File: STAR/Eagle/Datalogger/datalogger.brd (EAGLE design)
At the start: 26.4 x 55.9 mm, 9 parts, among them U1 MT25QL01GBBB8ESF-0AAT

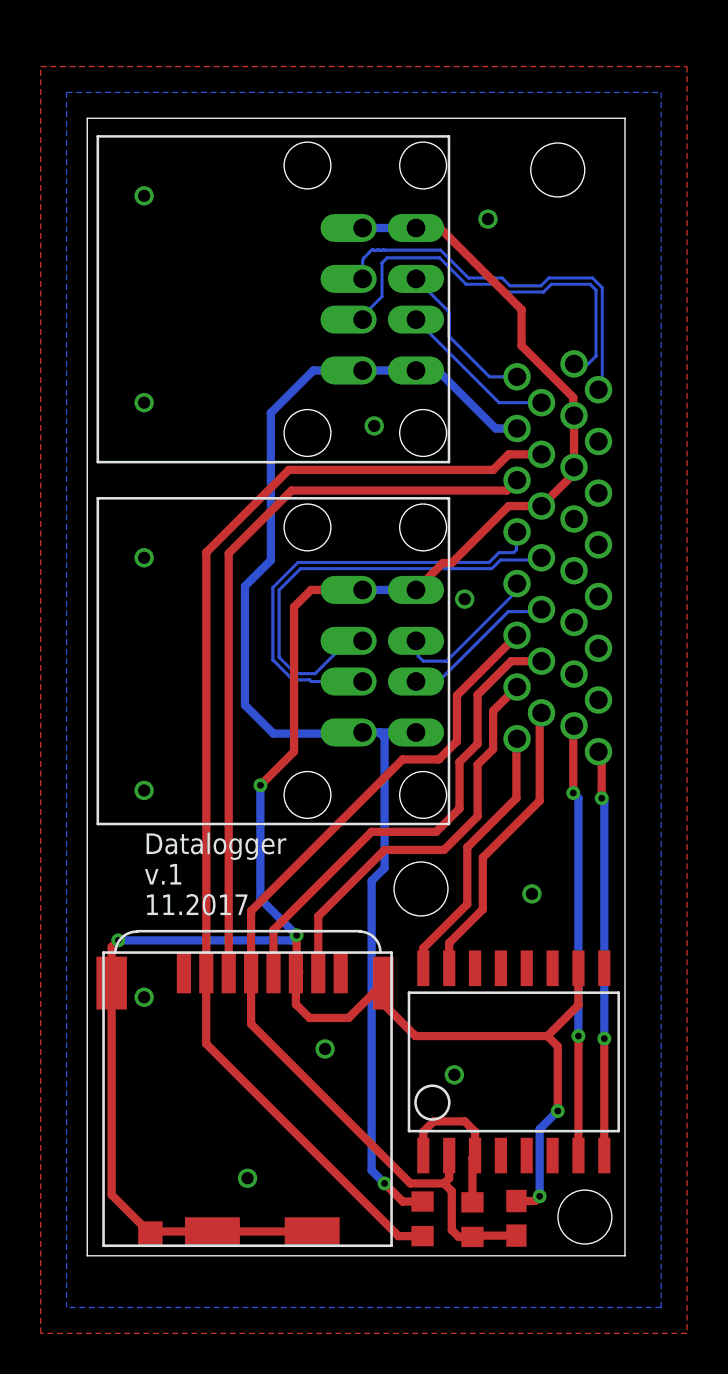
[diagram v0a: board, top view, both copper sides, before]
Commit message: fixed routing shit on datalogger:
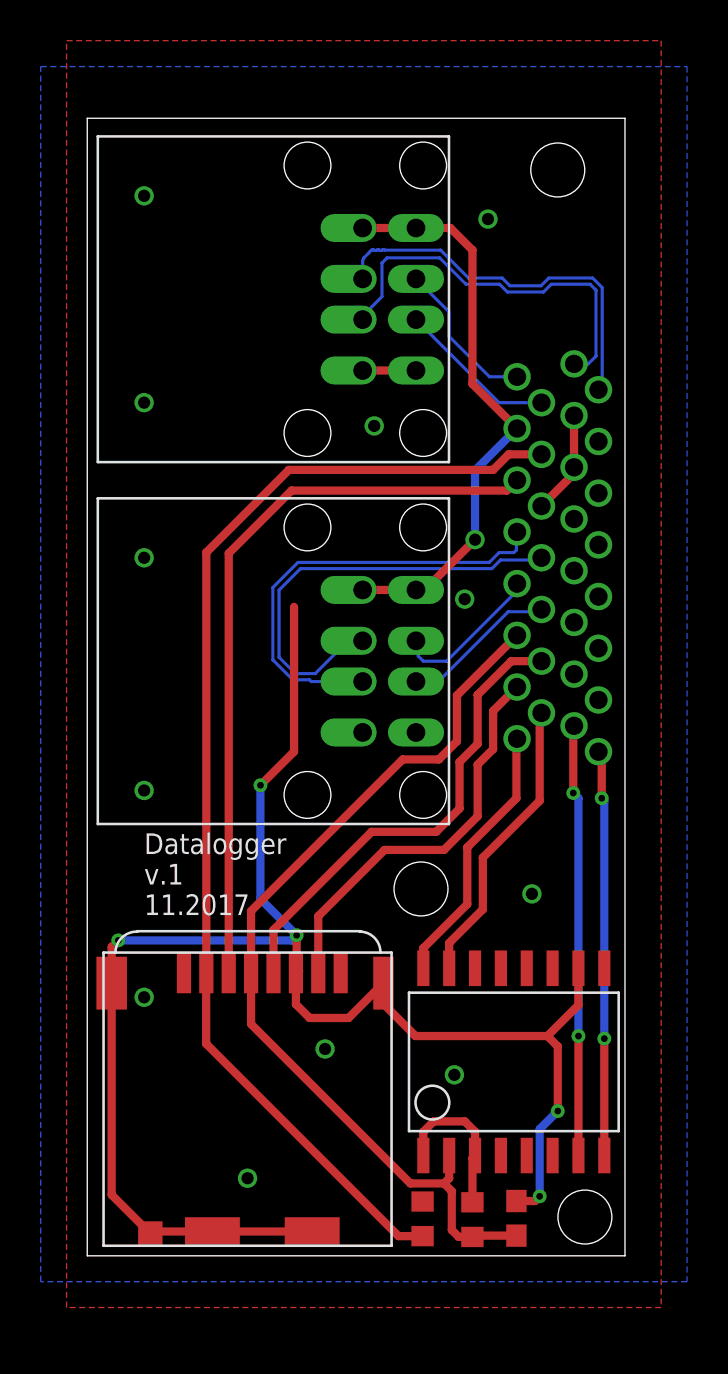
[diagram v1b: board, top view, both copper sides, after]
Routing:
- net +5V: track 63.0 -> 28.4 mm
- net GND: track 117.4 -> 90.1 mm
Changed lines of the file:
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@@
 </class>
 </classes>
-<designrules name="OshPark *">
+<designrules name="OshPark">
 <description language="de">&lt;b&gt;EAGLE Design Rules&lt;/b&gt;
 &lt;p&gt;
@@
 <param name="mlMinCreamFrame" value="0mil"/>
 <param name="mlMaxCreamFrame" value="0mil"/>
-<param name="mlViaStopLimit" value="25mil"/>
+<param name="mlViaStopLimit" value="0mil"/>
 <param name="srRoundness" value="0"/>
 <param name="srMinRoundness" value="0mil"/>
@@
 <contactref element="U$2" pad="GND1"/>
 <contactref element="CONNECTOR" pad="14"/>
-<wire x1="0.575" y1="35.25" x2="3.195" y2="35.25" width="0.4064" layer="16"/>
-<wire x1="0.575" y1="17.47" x2="3.195" y2="17.47" width="0.4064" layer="16"/>
 <wire x1="-2.7042" y1="-1.3447" x2="-2.7042" y2="-2.8838" width="0.4064" layer="1"/>
 <wire x1="-2.7042" y1="-2.8838" x2="-2.032" y2="-3.556" width="0.4064" layer="1"/>
@@
 <wire x1="-11.7542" y1="-1.8447" x2="-11.7542" y2="-12.2447" width="0.4064" layer="1"/>
 <wire x1="-11.7542" y1="-12.2447" x2="-9.8542" y2="-14.1447" width="0.4064" layer="1"/>
-<wire x1="3.195" y1="35.25" x2="4.374" y2="35.25" width="0.4064" layer="1"/>
-<wire x1="4.374" y1="35.25" x2="8.382" y2="31.242" width="0.4064" layer="1"/>
-<wire x1="8.382" y1="31.242" x2="8.382" y2="29.464" width="0.4064" layer="1"/>
-<wire x1="8.382" y1="29.464" x2="10.922" y2="26.924" width="0.4064" layer="1"/>
-<wire x1="10.922" y1="26.924" x2="10.922" y2="26.073" width="0.4064" layer="1"/>
 <wire x1="10.922" y1="26.073" x2="10.96" y2="26.035" width="0.4064" layer="1"/>
-<wire x1="9.36" y1="21.59" x2="7.747" y2="21.59" width="0.4064" layer="1"/>
-<wire x1="7.747" y1="21.59" x2="4.953" y2="18.796" width="0.4064" layer="1"/>
-<wire x1="4.953" y1="18.796" x2="4.521" y2="18.796" width="0.4064" layer="1"/>
-<wire x1="4.521" y1="18.796" x2="3.195" y2="17.47" width="0.4064" layer="1"/>
-<wire x1="0.575" y1="17.47" x2="-1.961" y2="17.47" width="0.4064" layer="1"/>
-<wire x1="-1.961" y1="17.47" x2="-2.794" y2="16.637" width="0.4064" layer="1"/>
 <wire x1="-2.794" y1="16.637" x2="-2.794" y2="9.525" width="0.4064" layer="1"/>
 <wire x1="-2.794" y1="9.525" x2="-4.445" y2="7.874" width="0.4064" layer="1"/>
@@
 <wire x1="9.271" y1="-12.319" x2="9.271" y2="-9.017" width="0.4064" layer="16"/>
 <wire x1="9.271" y1="-9.017" x2="10.16" y2="-8.128" width="0.4064" layer="16"/>
-<polygon width="0.4064" layer="1">
-<vertex x="-15.24" y="43.18"/>
-<vertex x="16.51" y="43.18"/>
-<vertex x="16.51" y="-19.05"/>
-<vertex x="-15.24" y="-19.05"/>
-</polygon>
-<polygon width="0.4064" layer="16">
-<vertex x="-13.97" y="41.91"/>
-<vertex x="15.24" y="41.91"/>
-<vertex x="15.24" y="-17.78"/>
-<vertex x="-13.97" y="-17.78"/>
-</polygon>
 <via x="-10.16" y="36.83" extent="1-16" drill="0.6"/>
 <via x="-10.16" y="26.67" extent="1-16" drill="0.6"/>
@@
 <via x="-5.08" y="-11.43" extent="1-16" drill="0.6"/>
 <via x="5.08" y="-6.35" extent="1-16" drill="0.6"/>
+<wire x1="0.575" y1="28.25" x2="3.195" y2="28.25" width="0.4064" layer="1"/>
+<polygon width="0.4064" layer="16">
+<vertex x="-15.24" y="43.18"/>
+<vertex x="16.51" y="43.18"/>
+<vertex x="16.51" y="-16.51"/>
+<vertex x="-15.24" y="-16.51"/>
+</polygon>
+<polygon width="0.4064" layer="1">
+<vertex x="-13.97" y="44.45"/>
+<vertex x="15.24" y="44.45"/>
+<vertex x="15.24" y="-17.78"/>
+<vertex x="-13.97" y="-17.78"/>
+</polygon>
 </signal>
 <signal name="+3V3">
@@
 <contactref element="R2" pad="2"/>
 <contactref element="CONNECTOR" pad="29"/>
-<wire x1="0.575" y1="28.25" x2="3.195" y2="28.25" width="0.4064" layer="16"/>
-<wire x1="3.195" y1="28.25" x2="4.262" y2="28.25" width="0.4064" layer="16"/>
-<wire x1="4.262" y1="28.25" x2="7.112" y2="25.4" width="0.4064" layer="16"/>
-<wire x1="7.112" y1="25.4" x2="8.16" y2="25.4" width="0.4064" layer="16"/>
-<wire x1="3.195" y1="10.47" x2="1.397" y2="10.47" width="0.4064" layer="16"/>
-<wire x1="1.397" y1="10.47" x2="0.575" y2="10.47" width="0.4064" layer="16"/>
-<wire x1="0.575" y1="28.25" x2="-1.849" y2="28.25" width="0.4064" layer="16"/>
-<wire x1="-1.849" y1="28.25" x2="-3.937" y2="26.162" width="0.4064" layer="16"/>
-<wire x1="-3.937" y1="26.162" x2="-3.937" y2="18.923" width="0.4064" layer="16"/>
-<wire x1="-3.937" y1="18.923" x2="-5.207" y2="17.653" width="0.4064" layer="16"/>
-<wire x1="-5.207" y1="17.653" x2="-5.207" y2="11.811" width="0.4064" layer="16"/>
-<wire x1="-5.207" y1="11.811" x2="-3.81" y2="10.414" width="0.4064" layer="16"/>
-<wire x1="-3.81" y1="10.414" x2="0.519" y2="10.414" width="0.4064" layer="16"/>
-<wire x1="0.519" y1="10.414" x2="0.575" y2="10.47" width="0.4064" layer="16"/>
-<wire x1="3.5179" y1="-12.5739" x2="2.5409" y2="-12.5739" width="0.4064" layer="1"/>
-<wire x1="2.5409" y1="-12.5739" x2="1.651" y2="-11.684" width="0.4064" layer="1"/>
-<via x="1.651" y="-11.684" extent="1-16" drill="0.3302"/>
-<wire x1="1.651" y1="10.216" x2="1.397" y2="10.47" width="0.4064" layer="16"/>
-<wire x1="1.651" y1="10.216" x2="1.651" y2="3.81" width="0.4064" layer="16"/>
-<wire x1="1.651" y1="3.81" x2="1.016" y2="3.175" width="0.4064" layer="16"/>
-<wire x1="1.016" y1="3.175" x2="1.016" y2="-11.049" width="0.4064" layer="16"/>
-<wire x1="1.016" y1="-11.049" x2="1.651" y2="-11.684" width="0.4064" layer="16"/>
+<wire x1="0.575" y1="35.25" x2="3.195" y2="35.25" width="0.4064" layer="1"/>
+<wire x1="3.195" y1="35.25" x2="4.882" y2="35.25" width="0.4064" layer="1"/>
+<wire x1="4.882" y1="35.25" x2="5.969" y2="34.163" width="0.4064" layer="1"/>
+<wire x1="5.969" y1="34.163" x2="5.969" y2="27.591" width="0.4064" layer="1"/>
+<wire x1="5.969" y1="27.591" x2="8.16" y2="25.4" width="0.4064" layer="1"/>
+<wire x1="3.195" y1="17.47" x2="0.575" y2="17.47" width="0.4064" layer="1"/>
+<wire x1="3.195" y1="17.47" x2="3.627" y2="17.47" width="0.4064" layer="1"/>
+<wire x1="3.627" y1="17.47" x2="6.096" y2="19.939" width="0.4064" layer="1"/>
+<via x="6.096" y="19.939" extent="1-16" drill="0.6"/>
+<wire x1="6.096" y1="19.939" x2="6.096" y2="23.336" width="0.4064" layer="16"/>
+<wire x1="6.096" y1="23.336" x2="8.16" y2="25.4" width="0.4064" layer="16"/>
+<wire x1="3.5179" y1="-12.5739" x2="3.627" y2="17.47" width="0" layer="19" extent="1-1"/>
 </signal>
 <signal name="DATA1_P">
@@
 </signal>
 </signals>
-<errors>
-</errors>
 </board>
 </drawing>

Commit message: datalogger v. 2
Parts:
- removed C1: 100nF, resistor:C0603
- removed CONNECTOR: J30J-31J30, CM_J30J:ZKN-31-J30
- removed R1: 4.7k, resistor:R0603
- removed U1: MT25QL01GBBB8ESF-0AAT, NR_IC:SOP2-16
- added J1: J30J-25, CM_J30J:ZKN-25
- added U$5: W25N01GV, NR_IC:WSON
- R2: value (none) -> 1M
- moved U$1 39.8 mm to (-7.62, 25.1)
- moved R2 35.5 mm to (0.00, 21.9), turned to 180 degrees
- moved U$4 20.5 mm to (11.1, -14.9), flipped to the top
- moved U$3 20.4 mm to (-5.08, 11.4)
- moved U$2 19.7 mm to (-5.08, -5.71)
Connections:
- removed net N$1: R1.2, U1.1, U1.3
- removed net N$10: CONNECTOR.11
- removed net N$12: CONNECTOR.13
- removed net N$2: CONNECTOR.3
- removed net N$3: CONNECTOR.4
- removed net N$4: CONNECTOR.5
- removed net N$5: CONNECTOR.6
- removed net N$6: CONNECTOR.7
- removed net N$7: CONNECTOR.8
- removed net N$8: CONNECTOR.9
- removed net N$9: CONNECTOR.10
- removed net PB23: CONNECTOR.2, U1.7
- new net B: J1.18
- new net F: J1.9
- new net H: J1.19
- new net J: J1.6
- new net R: J1.14
- new net S: J1.7
- new net V: J1.8
- new net Y: J1.10
- net +3V3: now also J1.12, U$5.P$8; no longer C1.1, CONNECTOR.21, R1.1, U1.2
- net +5V: now also J1.15; no longer CONNECTOR.29
- net DATA1_N: now also J1.2; no longer CONNECTOR.22
- net DATA1_P: now also J1.4; no longer CONNECTOR.23
- net DATA2_N: now also J1.23; no longer CONNECTOR.25
- net DATA2_P: now also J1.22; no longer CONNECTOR.24
- net DATA3_N: now also J1.16; no longer CONNECTOR.30
- net DATA3_P: now also J1.17; no longer CONNECTOR.31
- net DATA4_N: now also J1.21; no longer CONNECTOR.16
- net DATA4_P: now also J1.20; no longer CONNECTOR.15
- net GND: now also J1.13, U$5.P$1, U$5.P$4, U$5.P$PAD; no longer C1.2, CONNECTOR.12, CONNECTOR.14, CONNECTOR.26, U1.10
- net MISO_FLASH: now also J1.1, U$5.P$2; no longer CONNECTOR.1, U1.8
- net MISO_STAR: now also J1.25; no longer CONNECTOR.27
- net MOSI_FLASH: now also J1.3, U$5.P$5; no longer CONNECTOR.18, U1.15
- net MOSI_STAR: no longer CONNECTOR.19
- net SCK_FLASH: now also J1.5, U$5.P$6; no longer CONNECTOR.17, U1.16
- net SCK_STAR: now also J1.11; no longer CONNECTOR.20
- net SD_STAR: now also J1.24; no longer CONNECTOR.28
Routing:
- net GND: track 90.1 -> 0.00 mm, vias 17 -> 16
- net DATA2_P: track 22.0 -> 51.9 mm
- net DATA2_N: track 22.0 -> 52.0 mm
- net SD_STAR: track 57.1 -> 28.4 mm
- net DATA1_P: track 7.63 -> 31.8 mm
- net DATA1_N: track 7.63 -> 31.8 mm
- net MISO_STAR: track 36.3 -> 13.5 mm
- net PB23: track 21.2 -> 0.00 mm, vias 2 -> 0
- net MOSI_STAR: track 19.8 -> 0.00 mm
- net DATA4_P: track 19.2 -> 31.8 mm
- net DATA4_N: track 19.2 -> 31.8 mm
- net +5V: track 28.4 -> 38.5 mm, vias 1 -> 0
- net SCK_FLASH: track 13.2 -> 22.0 mm
- net MISO_FLASH: track 20.0 -> 28.4 mm, vias 2 -> 0
- net N$1: track 7.65 -> 0.00 mm
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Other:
- board text added: "1"
- board text added: "12.2017"
- board text added: "2"
- board text added: "3"
- board text added: "4"
- board text added: "Port 1"
- board text added: "Port 1, B: 2"
- board text added: "Port 1, T: 1"
- board text added: "Port 1, T: 3"
- board text added: "Port 1, T: 4"
- board text added: "Port 2"
- board text added: "v. 2"
- board text removed: "100nF"
- board text removed: "11.2017"
- board text removed: "1M"
- board text removed: "4.7k"
- board text removed: "B: Pi 2"
- board text removed: "B: Pi 4"
- board text removed: "T: Pi 1"
- board text removed: "T: Pi 3"
- board text removed: "v.1"
